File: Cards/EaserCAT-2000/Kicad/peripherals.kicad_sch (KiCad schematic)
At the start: 18 parts, among them J4 I2C bus2, J5 DAC1, J6 Encoder 1, J7 Encoder 2, J8 Encoder 3, J9 Encoder 4

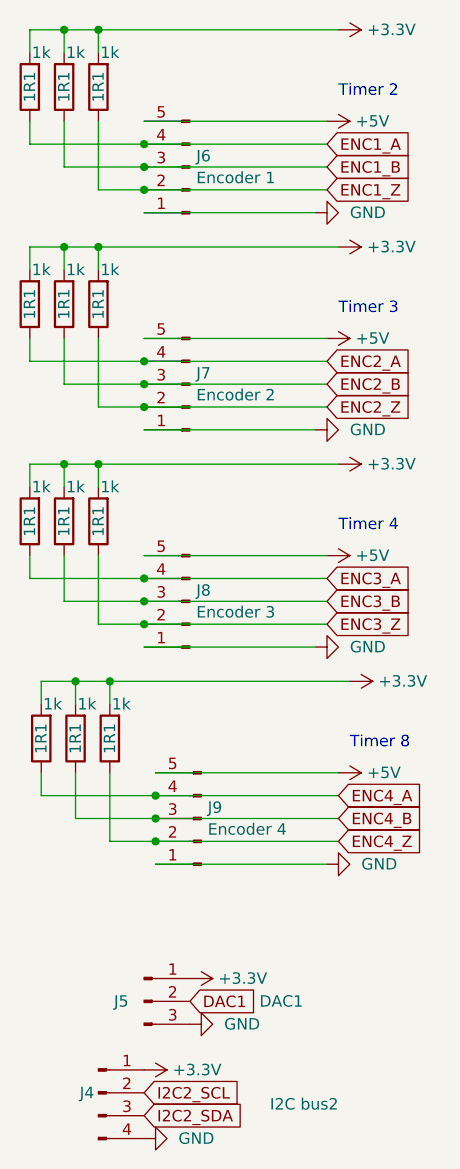
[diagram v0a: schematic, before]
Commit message: Moving all to Kicad8. Housekeeping symbols,libraries,3d-models
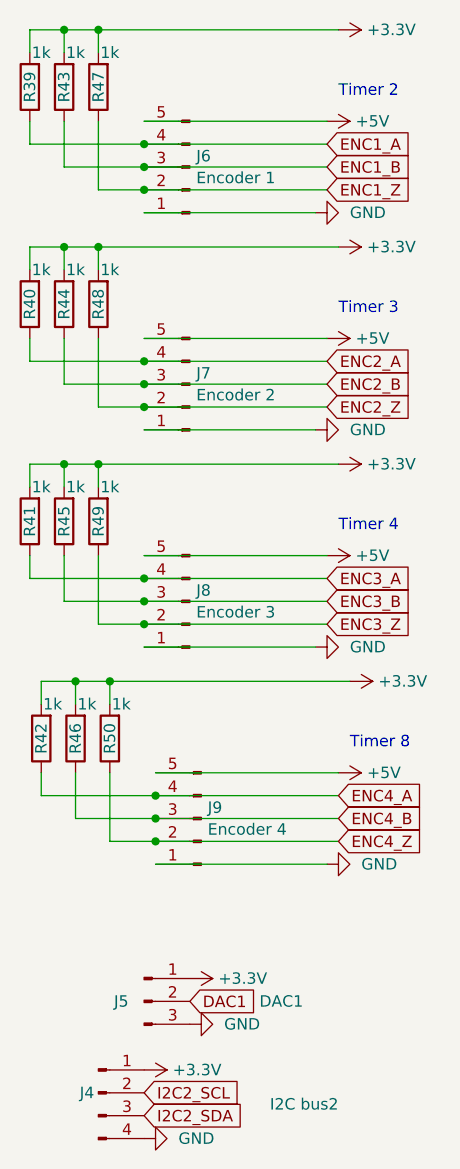
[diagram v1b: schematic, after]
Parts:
- renumbered 1R1 to R39, 1R1 to R40, 1R1 to R41, 1R1 to R42, 1R1 to R43, 1R1 to R44, 1R1 to R45, 1R1 to R46, 1R1 to R47, 1R1 to R48, 1R1 to R49, 1R1 to R50
